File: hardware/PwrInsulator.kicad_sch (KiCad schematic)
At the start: 6 parts, among them P1 AM1LS-0505S-NZ

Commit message: erased all traces, finished USB section, started HV section, swapped most footprints of R to be of the same type 0603 similary with caps (where it could be done), swapped optos for those used in Smart Fuses. Overall cleaned up the schematic of unnecessary circuitry ( gotta get that extra weight off ), also major rearragment of the components
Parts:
- C9: renamed from C8; footprint Capacitor_SMD:C_0805_2012Metric -> Capacitor_SMD:C_0603_1608Metric
- P2: renamed from P1; footprint PUTM_EV_BMS_footprint:AM1LS -> AM1LS:AM1LS
- R15: renamed from R13; footprint Resistor_SMD:R_1206_3216Metric -> Resistor_SMD:R_0603_1608Metric
- renumbered C1 to C2, L1 to L2, R11 to R12
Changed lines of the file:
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@@
   (symbol (lib_id "Device:L") (at 123.825 88.265 90)
     (in_bom yes) (on_board yes)
-    (property "Reference" "L1" (id 0) (at 123.825 83.439 90))
+    (property "Reference" "L2" (id 0) (at 123.825 83.439 90))
     (property "Value" "6.8uH" (id 1) (at 123.825 85.7504 90))
     (property "Footprint" "Inductor_SMD:L_1206_3216Metric" (id 2) (at 123.825 88.265 0)
@@
   (symbol (lib_id "PUTM_EV_BMS_library:AM1LS-0505S-NZ") (at 142.875 93.345 0)
     (in_bom yes) (on_board yes)
-    (property "Reference" "P1" (id 0) (at 142.875 81.534 0))
+    (property "Reference" "P2" (id 0) (at 142.875 81.534 0))
     (property "Value" "AM1LS-0505S-NZ" (id 1) (at 142.875 83.8454 0))
-    (property "Footprint" "PUTM_EV_BMS_footprint:AM1LS" (id 2) (at 142.875 93.345 0)
+    (property "Footprint" "AM1LS:AM1LS" (id 2) (at 142.875 93.345 0)
       (effects (font (size 1.27 1.27)) hide)
     )
@@
   (symbol (lib_id "Device:C_Small") (at 128.905 93.345 0)
     (in_bom yes) (on_board yes)
-    (property "Reference" "C1" (id 0) (at 123.19 92.075 0)
+    (property "Reference" "C2" (id 0) (at 123.19 92.075 0)
       (effects (font (size 1.27 1.27)) (justify left))
     )
@@
   (symbol (lib_id "Device:R") (at 160.655 88.265 90)
     (in_bom yes) (on_board yes)
-    (property "Reference" "R11" (id 0) (at 158.75 85.725 90)
+    (property "Reference" "R12" (id 0) (at 158.75 85.725 90)
       (effects (font (size 1.27 1.27)) (justify right))
     )
@@
   (symbol (lib_id "Device:R") (at 174.625 93.345 180)
     (in_bom yes) (on_board yes)
-    (property "Reference" "R13" (id 0) (at 176.403 92.1766 0)
+    (property "Reference" "R15" (id 0) (at 176.403 92.1766 0)
       (effects (font (size 1.27 1.27)) (justify right))
     )
@@
       (effects (font (size 1.27 1.27)) (justify right))
     )
-    (property "Footprint" "Resistor_SMD:R_1206_3216Metric" (id 2) (at 176.403 93.345 90)
+    (property "Footprint" "Resistor_SMD:R_0603_1608Metric" (id 2) (at 176.403 93.345 90)
       (effects (font (size 1.27 1.27)) hide)
     )
@@
   (symbol (lib_id "Device:C_Small") (at 165.735 93.345 0)
     (in_bom yes) (on_board yes)
-    (property "Reference" "C8" (id 0) (at 168.0718 92.1766 0)
+    (property "Reference" "C9" (id 0) (at 168.0718 92.1766 0)
       (effects (font (size 1.27 1.27)) (justify left))
     )
@@
       (effects (font (size 1.27 1.27)) (justify left))
     )
-    (property "Footprint" "Capacitor_SMD:C_0805_2012Metric" (id 2) (at 165.735 93.345 0)
+    (property "Footprint" "Capacitor_SMD:C_0603_1608Metric" (id 2) (at 165.735 93.345 0)
       (effects (font (size 1.27 1.27)) hide)
     )

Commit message: 3d models update, more work on pcb
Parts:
- renumbered C2 to C1, C9 to C8, L2 to L1, P2 to P1, R12 to R11, R15 to R13
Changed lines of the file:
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@@
   (symbol (lib_id "Device:L") (at 123.825 88.265 90)
     (in_bom yes) (on_board yes)
-    (property "Reference" "L2" (id 0) (at 123.825 83.439 90))
+    (property "Reference" "L1" (id 0) (at 123.825 83.439 90))
     (property "Value" "6.8uH" (id 1) (at 123.825 85.7504 90))
     (property "Footprint" "Inductor_SMD:L_1206_3216Metric" (id 2) (at 123.825 88.265 0)
@@
   (symbol (lib_id "PUTM_EV_BMS_library:AM1LS-0505S-NZ") (at 142.875 93.345 0)
     (in_bom yes) (on_board yes)
-    (property "Reference" "P2" (id 0) (at 142.875 81.534 0))
+    (property "Reference" "P1" (id 0) (at 142.875 81.534 0))
     (property "Value" "AM1LS-0505S-NZ" (id 1) (at 142.875 83.8454 0))
     (property "Footprint" "AM1LS:AM1LS" (id 2) (at 142.875 93.345 0)
@@
   (symbol (lib_id "Device:C_Small") (at 128.905 93.345 0)
     (in_bom yes) (on_board yes)
-    (property "Reference" "C2" (id 0) (at 123.19 92.075 0)
+    (property "Reference" "C1" (id 0) (at 123.19 92.075 0)
       (effects (font (size 1.27 1.27)) (justify left))
     )
@@
   (symbol (lib_id "Device:R") (at 160.655 88.265 90)
     (in_bom yes) (on_board yes)
-    (property "Reference" "R12" (id 0) (at 158.75 85.725 90)
+    (property "Reference" "R11" (id 0) (at 158.75 85.725 90)
       (effects (font (size 1.27 1.27)) (justify right))
     )
@@
   (symbol (lib_id "Device:R") (at 174.625 93.345 180)
     (in_bom yes) (on_board yes)
-    (property "Reference" "R15" (id 0) (at 176.403 92.1766 0)
+    (property "Reference" "R13" (id 0) (at 176.403 92.1766 0)
       (effects (font (size 1.27 1.27)) (justify right))
     )
@@
   (symbol (lib_id "Device:C_Small") (at 165.735 93.345 0)
     (in_bom yes) (on_board yes)
-    (property "Reference" "C9" (id 0) (at 168.0718 92.1766 0)
+    (property "Reference" "C8" (id 0) (at 168.0718 92.1766 0)
       (effects (font (size 1.27 1.27)) (justify left))
     )

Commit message: remade pcb so it fits into 100 x 100 mm and some minor modifications
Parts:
- renumbered C1 to C2, C8 to C9, L1 to L2, P1 to P2, R11 to R12, R13 to R15
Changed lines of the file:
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@@
   (symbol (lib_id "Device:L") (at 123.825 88.265 90)
     (in_bom yes) (on_board yes)
-    (property "Reference" "L1" (id 0) (at 123.825 83.439 90))
+    (property "Reference" "L2" (id 0) (at 123.825 83.439 90))
     (property "Value" "6.8uH" (id 1) (at 123.825 85.7504 90))
     (property "Footprint" "Inductor_SMD:L_1206_3216Metric" (id 2) (at 123.825 88.265 0)
@@
   (symbol (lib_id "PUTM_EV_BMS_library:AM1LS-0505S-NZ") (at 142.875 93.345 0)
     (in_bom yes) (on_board yes)
-    (property "Reference" "P1" (id 0) (at 142.875 81.534 0))
+    (property "Reference" "P2" (id 0) (at 142.875 81.534 0))
     (property "Value" "AM1LS-0505S-NZ" (id 1) (at 142.875 83.8454 0))
     (property "Footprint" "AM1LS:AM1LS" (id 2) (at 142.875 93.345 0)
@@
   (symbol (lib_id "Device:C_Small") (at 128.905 93.345 0)
     (in_bom yes) (on_board yes)
-    (property "Reference" "C1" (id 0) (at 123.19 92.075 0)
+    (property "Reference" "C2" (id 0) (at 123.19 92.075 0)
       (effects (font (size 1.27 1.27)) (justify left))
     )
@@
   (symbol (lib_id "Device:R") (at 160.655 88.265 90)
     (in_bom yes) (on_board yes)
-    (property "Reference" "R11" (id 0) (at 158.75 85.725 90)
+    (property "Reference" "R12" (id 0) (at 158.75 85.725 90)
       (effects (font (size 1.27 1.27)) (justify right))
     )
@@
   (symbol (lib_id "Device:R") (at 174.625 93.345 180)
     (in_bom yes) (on_board yes)
-    (property "Reference" "R13" (id 0) (at 176.403 92.1766 0)
+    (property "Reference" "R15" (id 0) (at 176.403 92.1766 0)
       (effects (font (size 1.27 1.27)) (justify right))
     )
@@
   (symbol (lib_id "Device:C_Small") (at 165.735 93.345 0)
     (in_bom yes) (on_board yes)
-    (property "Reference" "C8" (id 0) (at 168.0718 92.1766 0)
+    (property "Reference" "C9" (id 0) (at 168.0718 92.1766 0)
       (effects (font (size 1.27 1.27)) (justify left))
     )

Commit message: schematic override, just cuz
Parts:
- renumbered C2 to C1, C9 to C2, L2 to L1, P2 to P1, R12 to R11, R15 to R12
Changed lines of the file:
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@@
   (symbol (lib_id "Device:L") (at 123.825 88.265 90)
     (in_bom yes) (on_board yes)
-    (property "Reference" "L2" (id 0) (at 123.825 83.439 90))
+    (property "Reference" "L1" (id 0) (at 123.825 83.439 90))
     (property "Value" "6.8uH" (id 1) (at 123.825 85.7504 90))
     (property "Footprint" "Inductor_SMD:L_1206_3216Metric" (id 2) (at 123.825 88.265 0)
@@
   (symbol (lib_id "PUTM_EV_BMS_library:AM1LS-0505S-NZ") (at 142.875 93.345 0)
     (in_bom yes) (on_board yes)
-    (property "Reference" "P2" (id 0) (at 142.875 81.534 0))
+    (property "Reference" "P1" (id 0) (at 142.875 81.534 0))
     (property "Value" "AM1LS-0505S-NZ" (id 1) (at 142.875 83.8454 0))
     (property "Footprint" "AM1LS:AM1LS" (id 2) (at 142.875 93.345 0)
       (effects (font (size 1.27 1.27)) hide)
     )
-    (property "Datasheet" "https://www.tme.eu/Document/eb524b8882472c891796e11a1a1007e6/am1ls-%28j%29nz.pdf" (id 3) (at 142.875 93.345 0)
+    (property "Datasheet" "http://www.aimtec.com/site/Aimtec/files/Datasheet/HighResolution/am1ls-nz-e.pdf?ft4=16-887" (id 3) (at 142.875 93.345 0)
       (effects (font (size 1.27 1.27)) hide)
     )
@@
   (symbol (lib_id "Device:C_Small") (at 128.905 93.345 0)
     (in_bom yes) (on_board yes)
-    (property "Reference" "C2" (id 0) (at 123.19 92.075 0)
+    (property "Reference" "C1" (id 0) (at 123.19 92.075 0)
       (effects (font (size 1.27 1.27)) (justify left))
     )
@@
   (symbol (lib_id "Device:R") (at 160.655 88.265 90)
     (in_bom yes) (on_board yes)
-    (property "Reference" "R12" (id 0) (at 158.75 85.725 90)
+    (property "Reference" "R11" (id 0) (at 158.75 85.725 90)
       (effects (font (size 1.27 1.27)) (justify right))
     )
@@
   (symbol (lib_id "Device:R") (at 174.625 93.345 180)
     (in_bom yes) (on_board yes)
-    (property "Reference" "R15" (id 0) (at 176.403 92.1766 0)
+    (property "Reference" "R12" (id 0) (at 176.403 92.1766 0)
       (effects (font (size 1.27 1.27)) (justify right))
     )
@@
   (symbol (lib_id "Device:C_Small") (at 165.735 93.345 0)
     (in_bom yes) (on_board yes)
-    (property "Reference" "C9" (id 0) (at 168.0718 92.1766 0)
+    (property "Reference" "C2" (id 0) (at 168.0718 92.1766 0)
       (effects (font (size 1.27 1.27)) (justify left))
     )

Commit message: changed HV measurements from isolated opamp to isolated ADC with isolated spi communication, changed safety laatching from mosfet back to relay
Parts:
- renumbered C1 to C8, C2 to C9, L1 to L2, P1 to P2, R11 to R13, R12 to R15
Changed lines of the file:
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@@
   (symbol (lib_id "Device:L") (at 123.825 88.265 90)
     (in_bom yes) (on_board yes)
-    (property "Reference" "L1" (id 0) (at 123.825 83.439 90))
+    (property "Reference" "L2" (id 0) (at 123.825 83.439 90))
     (property "Value" "6.8uH" (id 1) (at 123.825 85.7504 90))
     (property "Footprint" "Inductor_SMD:L_1206_3216Metric" (id 2) (at 123.825 88.265 0)
@@
   (symbol (lib_id "PUTM_EV_BMS_library:AM1LS-0505S-NZ") (at 142.875 93.345 0)
     (in_bom yes) (on_board yes)
-    (property "Reference" "P1" (id 0) (at 142.875 81.534 0))
+    (property "Reference" "P2" (id 0) (at 142.875 81.534 0))
     (property "Value" "AM1LS-0505S-NZ" (id 1) (at 142.875 83.8454 0))
     (property "Footprint" "AM1LS:AM1LS" (id 2) (at 142.875 93.345 0)
@@
   (symbol (lib_id "Device:C_Small") (at 128.905 93.345 0)
     (in_bom yes) (on_board yes)
-    (property "Reference" "C1" (id 0) (at 123.19 92.075 0)
+    (property "Reference" "C8" (id 0) (at 123.19 92.075 0)
       (effects (font (size 1.27 1.27)) (justify left))
     )
@@
   (symbol (lib_id "Device:R") (at 160.655 88.265 90)
     (in_bom yes) (on_board yes)
-    (property "Reference" "R11" (id 0) (at 158.75 85.725 90)
+    (property "Reference" "R13" (id 0) (at 158.75 85.725 90)
       (effects (font (size 1.27 1.27)) (justify right))
     )
@@
   (symbol (lib_id "Device:R") (at 174.625 93.345 180)
     (in_bom yes) (on_board yes)
-    (property "Reference" "R12" (id 0) (at 176.403 92.1766 0)
+    (property "Reference" "R15" (id 0) (at 176.403 92.1766 0)
       (effects (font (size 1.27 1.27)) (justify right))
     )
@@
   (symbol (lib_id "Device:C_Small") (at 165.735 93.345 0)
     (in_bom yes) (on_board yes)
-    (property "Reference" "C2" (id 0) (at 168.0718 92.1766 0)
+    (property "Reference" "C9" (id 0) (at 168.0718 92.1766 0)
       (effects (font (size 1.27 1.27)) (justify left))
     )

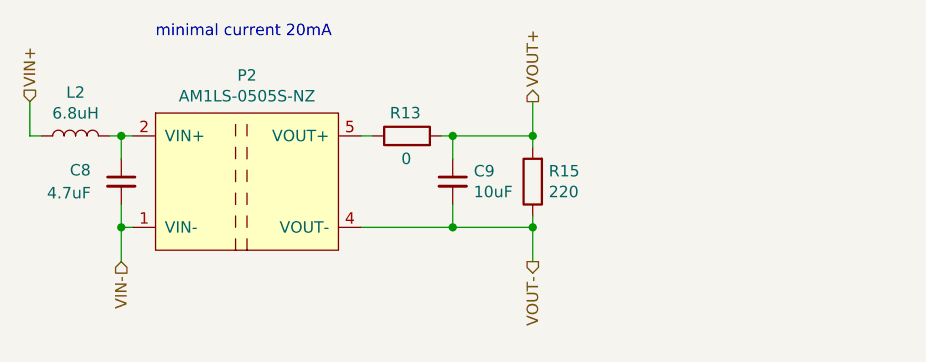
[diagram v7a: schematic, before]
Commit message: changed the 1V voltage ref made from RL circuit to low noise, 0.1% error 1.024 V ref gen, and changed the opamp used for current sensor feedback filtration to a high precision low drift opamp
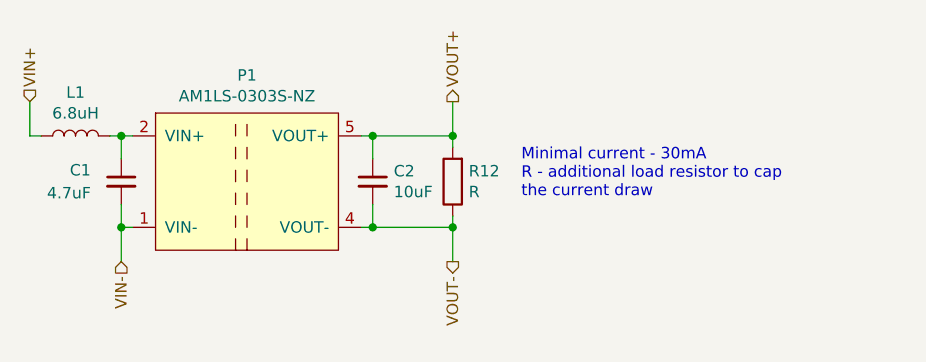
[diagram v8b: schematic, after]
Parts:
- removed R13: 0, Resistor_SMD:R_0603_1608Metric, symbol Device:R
- P1: renamed from P2; value AM1LS-0505S-NZ -> AM1LS-0303S-NZ
- R12: renamed from R15; value 220 -> R
- renumbered C8 to C1, C9 to C2, L2 to L1
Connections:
- net VOUT+: now also P1.5 (VOUT+)
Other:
- note added: "Minimal current - 30mA R - additional load resistor to cap the current draw"
- note removed: "minimal current 20mA"
- moved on the sheet: C2, R12
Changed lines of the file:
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@@
   (junction (at 128.905 98.425) (diameter 0) (color 0 0 0 0)
+  )
+  (junction (at 156.845 88.265) (diameter 0) (color 0 0 0 0)
   )
   (junction (at 165.735 88.265) (diameter 0) (color 0 0 0 0)
   )
-  (junction (at 174.625 88.265) (diameter 0) (color 0 0 0 0)
+  (junction (at 128.905 88.265) (diameter 0) (color 0 0 0 0)
   )
-  (junction (at 128.905 88.265) (diameter 0) (color 0 0 0 0)
+  (junction (at 156.845 98.425) (diameter 0) (color 0 0 0 0)
   )
   (junction (at 165.735 98.425) (diameter 0) (color 0 0 0 0)
   )
-  (junction (at 174.625 98.425) (diameter 0) (color 0 0 0 0)
-  )
-  (wire (pts (xy 165.735 88.265) (xy 174.625 88.265))
+  (wire (pts (xy 156.845 88.265) (xy 165.735 88.265))
     (stroke (width 0) (type default) (color 0 0 0 0))
   )
@@
     (stroke (width 0) (type default) (color 0 0 0 0))
   )
-  (wire (pts (xy 174.625 98.425) (xy 174.625 102.235))
+  (wire (pts (xy 165.735 98.425) (xy 165.735 102.235))
     (stroke (width 0) (type default) (color 0 0 0 0))
   )
@@
     (stroke (width 0) (type default) (color 0 0 0 0))
   )
-  (wire (pts (xy 174.625 89.535) (xy 174.625 88.265))
+  (wire (pts (xy 165.735 89.535) (xy 165.735 88.265))
     (stroke (width 0) (type default) (color 0 0 0 0))
   )
-  (wire (pts (xy 174.625 98.425) (xy 165.735 98.425))
+  (wire (pts (xy 155.575 88.265) (xy 156.845 88.265))
+    (stroke (width 0) (type default) (color 0 0 0 0))
+  )
+  (wire (pts (xy 156.845 98.425) (xy 165.735 98.425))
     (stroke (width 0) (type default) (color 0 0 0 0))
   )
@@
     (stroke (width 0) (type default) (color 0 0 0 0))
   )
-  (wire (pts (xy 155.575 88.265) (xy 156.845 88.265))
-    (stroke (width 0) (type default) (color 0 0 0 0))
-  )
-  (wire (pts (xy 165.735 88.265) (xy 165.735 90.805))
+  (wire (pts (xy 156.845 88.265) (xy 156.845 90.805))
     (stroke (width 0) (type default) (color 0 0 0 0))
   )
@@
     (stroke (width 0) (type default) (color 0 0 0 0))
   )
-  (wire (pts (xy 164.465 88.265) (xy 165.735 88.265))
+  (wire (pts (xy 156.845 95.885) (xy 156.845 98.425))
     (stroke (width 0) (type default) (color 0 0 0 0))
   )
-  (wire (pts (xy 165.735 98.425) (xy 155.575 98.425))
-    (stroke (width 0) (type default) (color 0 0 0 0))
-  )
-  (wire (pts (xy 165.735 95.885) (xy 165.735 98.425))
-    (stroke (width 0) (type default) (color 0 0 0 0))
-  )
-  (wire (pts (xy 174.625 84.455) (xy 174.625 88.265))
+  (wire (pts (xy 165.735 84.455) (xy 165.735 88.265))
     (stroke (width 0) (type default) (color 0 0 0 0))
   )
@@
     (stroke (width 0) (type default) (color 0 0 0 0))
   )
-  (wire (pts (xy 174.625 97.155) (xy 174.625 98.425))
+  (wire (pts (xy 156.845 98.425) (xy 155.575 98.425))
     (stroke (width 0) (type default) (color 0 0 0 0))
   )
-  (text "minimal current 20mA" (at 132.715 77.47 0)
+  (wire (pts (xy 165.735 97.155) (xy 165.735 98.425))
+    (stroke (width 0) (type default) (color 0 0 0 0))
+  )
+  (text "Minimal current - 30mA\nR - additional load resistor to cap\nthe current draw"
+    (at 173.355 95.25 0)
     (effects (font (size 1.27 1.27)) (justify left bottom))
   )
@@
     (effects (font (size 1.27 1.27)) (justify right))
   )
-  (hierarchical_label "VOUT-" (shape output) (at 174.625 102.235 270)
+  (hierarchical_label "VOUT-" (shape output) (at 165.735 102.235 270)
     (effects (font (size 1.27 1.27)) (justify right))
   )
-  (hierarchical_label "VOUT+" (shape output) (at 174.625 84.455 90)
+  (hierarchical_label "VOUT+" (shape output) (at 165.735 84.455 90)
     (effects (font (size 1.27 1.27)) (justify left))
   )
   (symbol (lib_id "Device:L") (at 123.825 88.265 90)
     (in_bom yes) (on_board yes)
-    (property "Reference" "L2" (id 0) (at 123.825 83.439 90))
+    (property "Reference" "L1" (id 0) (at 123.825 83.439 90))
     (property "Value" "6.8uH" (id 1) (at 123.825 85.7504 90))
     (property "Footprint" "Inductor_SMD:L_1206_3216Metric" (id 2) (at 123.825 88.265 0)
@@
   (symbol (lib_id "PUTM_EV_BMS_library:AM1LS-0505S-NZ") (at 142.875 93.345 0)
     (in_bom yes) (on_board yes)
-    (property "Reference" "P2" (id 0) (at 142.875 81.534 0))
-    (property "Value" "AM1LS-0505S-NZ" (id 1) (at 142.875 83.8454 0))
+    (property "Reference" "P1" (id 0) (at 142.875 81.534 0))
+    (property "Value" "AM1LS-0303S-NZ" (id 1) (at 142.875 83.8454 0))
     (property "Footprint" "AM1LS:AM1LS" (id 2) (at 142.875 93.345 0)
       (effects (font (size 1.27 1.27)) hide)
@@
   (symbol (lib_id "Device:C_Small") (at 128.905 93.345 0)
     (in_bom yes) (on_board yes)
-    (property "Reference" "C8" (id 0) (at 123.19 92.075 0)
+    (property "Reference" "C1" (id 0) (at 123.19 92.075 0)
       (effects (font (size 1.27 1.27)) (justify left))
     )
@@
     (pin "2")
   )
-  (symbol (lib_id "Device:R") (at 160.655 88.265 90)
+  (symbol (lib_id "Device:R") (at 165.735 93.345 180)
     (in_bom yes) (on_board yes)
-    (property "Reference" "R13" (id 0) (at 158.75 85.725 90)
+    (property "Reference" "R12" (id 0) (at 167.513 92.1766 0)
       (effects (font (size 1.27 1.27)) (justify right))
     )
-    (property "Value" "0" (id 1) (at 160.02 90.805 90)
+    (property "Value" "R" (id 1) (at 167.513 94.488 0)
       (effects (font (size 1.27 1.27)) (justify right))
     )
-    (property "Footprint" "Resistor_SMD:R_0603_1608Metric" (id 2) (at 160.655 90.043 90)
+    (property "Footprint" "Resistor_SMD:R_0603_1608Metric" (id 2) (at 167.513 93.345 90)
       (effects (font (size 1.27 1.27)) hide)
     )
-    (property "Datasheet" "~" (id 3) (at 160.655 88.265 0)
+    (property "Datasheet" "~" (id 3) (at 165.735 93.345 0)
       (effects (font (size 1.27 1.27)) hide)
     )
@@
     (pin "2")
   )
-  (symbol (lib_id "Device:R") (at 174.625 93.345 180)
+  (symbol (lib_id "Device:C_Small") (at 156.845 93.345 0)
     (in_bom yes) (on_board yes)
-    (property "Reference" "R15" (id 0) (at 176.403 92.1766 0)
-      (effects (font (size 1.27 1.27)) (justify right))
+    (property "Reference" "C2" (id 0) (at 159.1818 92.1766 0)
+      (effects (font (size 1.27 1.27)) (justify left))
     )
-    (property "Value" "220" (id 1) (at 176.403 94.488 0)
-      (effects (font (size 1.27 1.27)) (justify right))
+    (property "Value" "10uF" (id 1) (at 159.1818 94.488 0)
+      (effects (font (size 1.27 1.27)) (justify left))
     )
-    (property "Footprint" "Resistor_SMD:R_0603_1608Metric" (id 2) (at 176.403 93.345 90)
+    (property "Footprint" "Capacitor_SMD:C_0603_1608Metric" (id 2) (at 156.845 93.345 0)
       (effects (font (size 1.27 1.27)) hide)
     )
-    (property "Datasheet" "~" (id 3) (at 174.625 93.345 0)
+    (property "Datasheet" "~" (id 3) (at 156.845 93.345 0)
       (effects (font (size 1.27 1.27)) hide)
     )
-    (pin "1")
-    (pin "2")
-  )
-  (symbol (lib_id "Device:C_Small") (at 165.735 93.345 0)
-    (in_bom yes) (on_board yes)
-    (property "Reference" "C9" (id 0) (at 168.0718 92.1766 0)
-      (effects (font (size 1.27 1.27)) (justify left))
-    )
-    (property "Value" "10uF" (id 1) (at 168.0718 94.488 0)
-      (effects (font (size 1.27 1.27)) (justify left))
-    )
-    (property "Footprint" "Capacitor_SMD:C_0603_1608Metric" (id 2) (at 165.735 93.345 0)
-      (effects (font (size 1.27 1.27)) hide)
-    )
-    (property "Datasheet" "~" (id 3) (at 165.735 93.345 0)
-      (effects (font (size 1.27 1.27)) hide)
-    )
